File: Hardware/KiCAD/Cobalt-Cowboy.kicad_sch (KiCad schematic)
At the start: 1 part, among them J3 USB_C_Receptacle

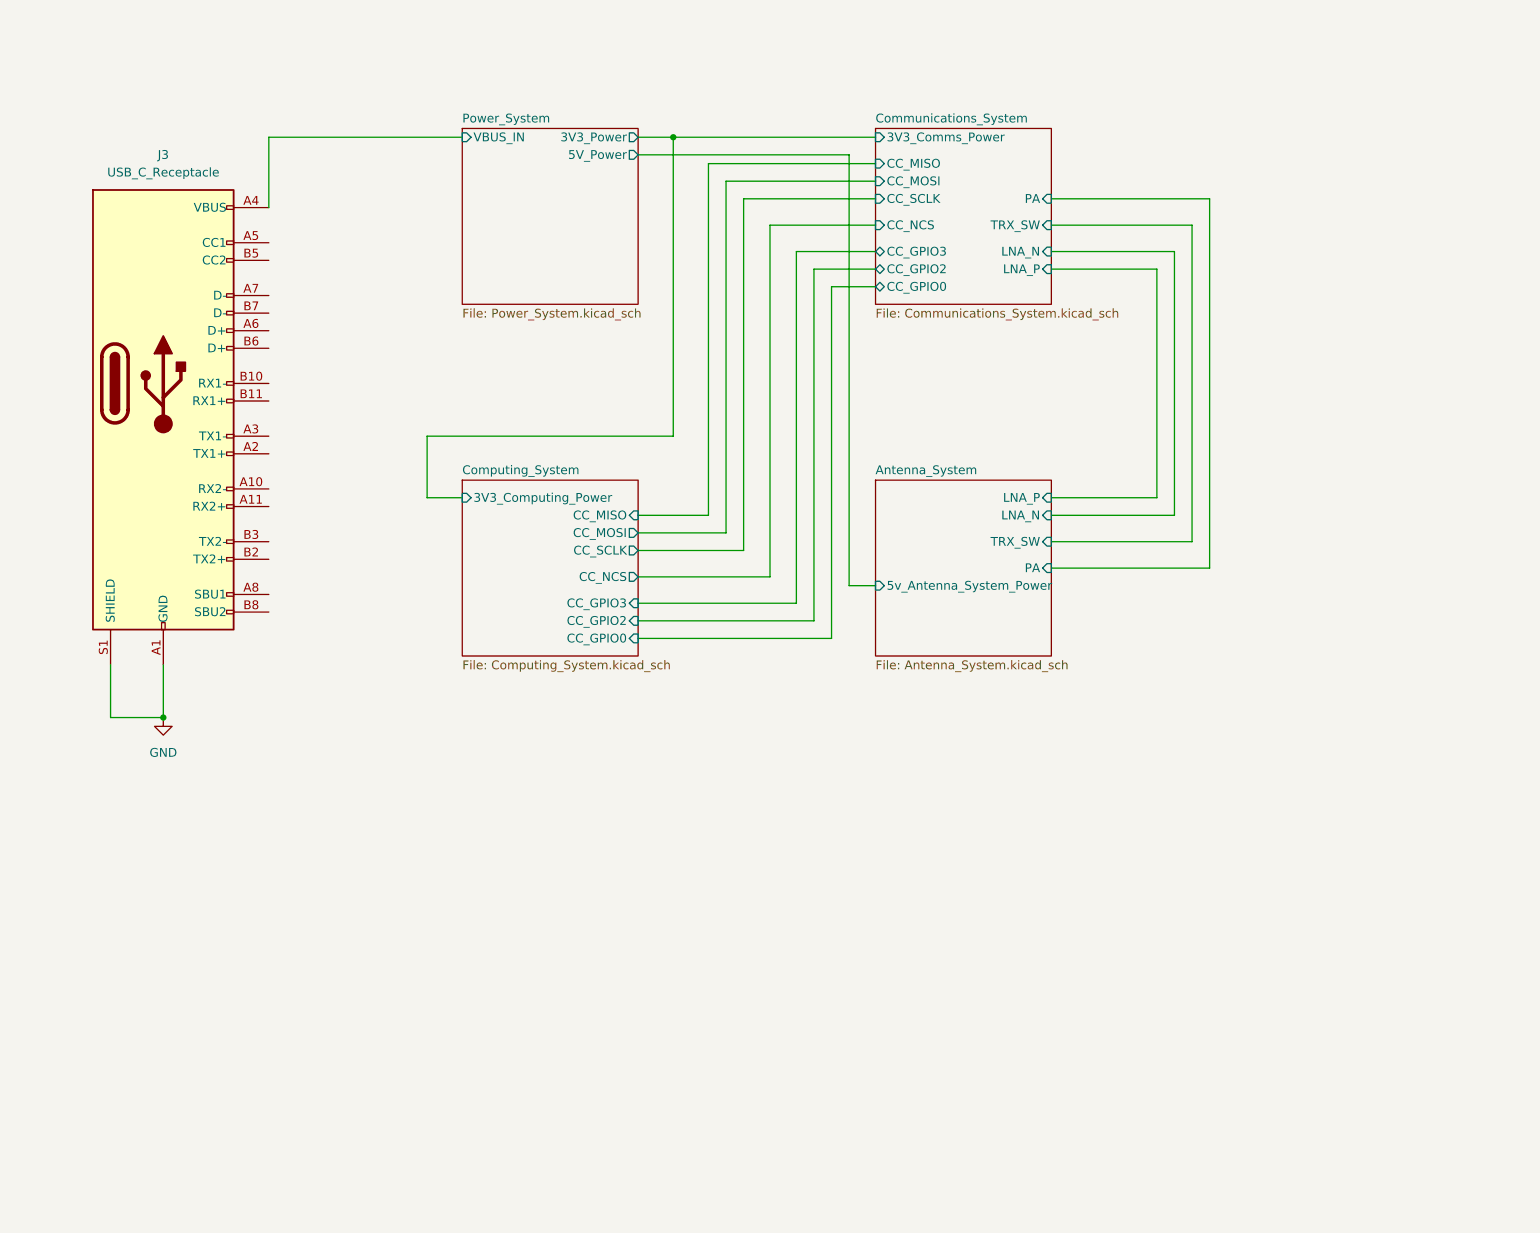
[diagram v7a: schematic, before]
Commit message: feat: subsystem exploration, begin placement, routing #11 #12 #4 many new project symbols
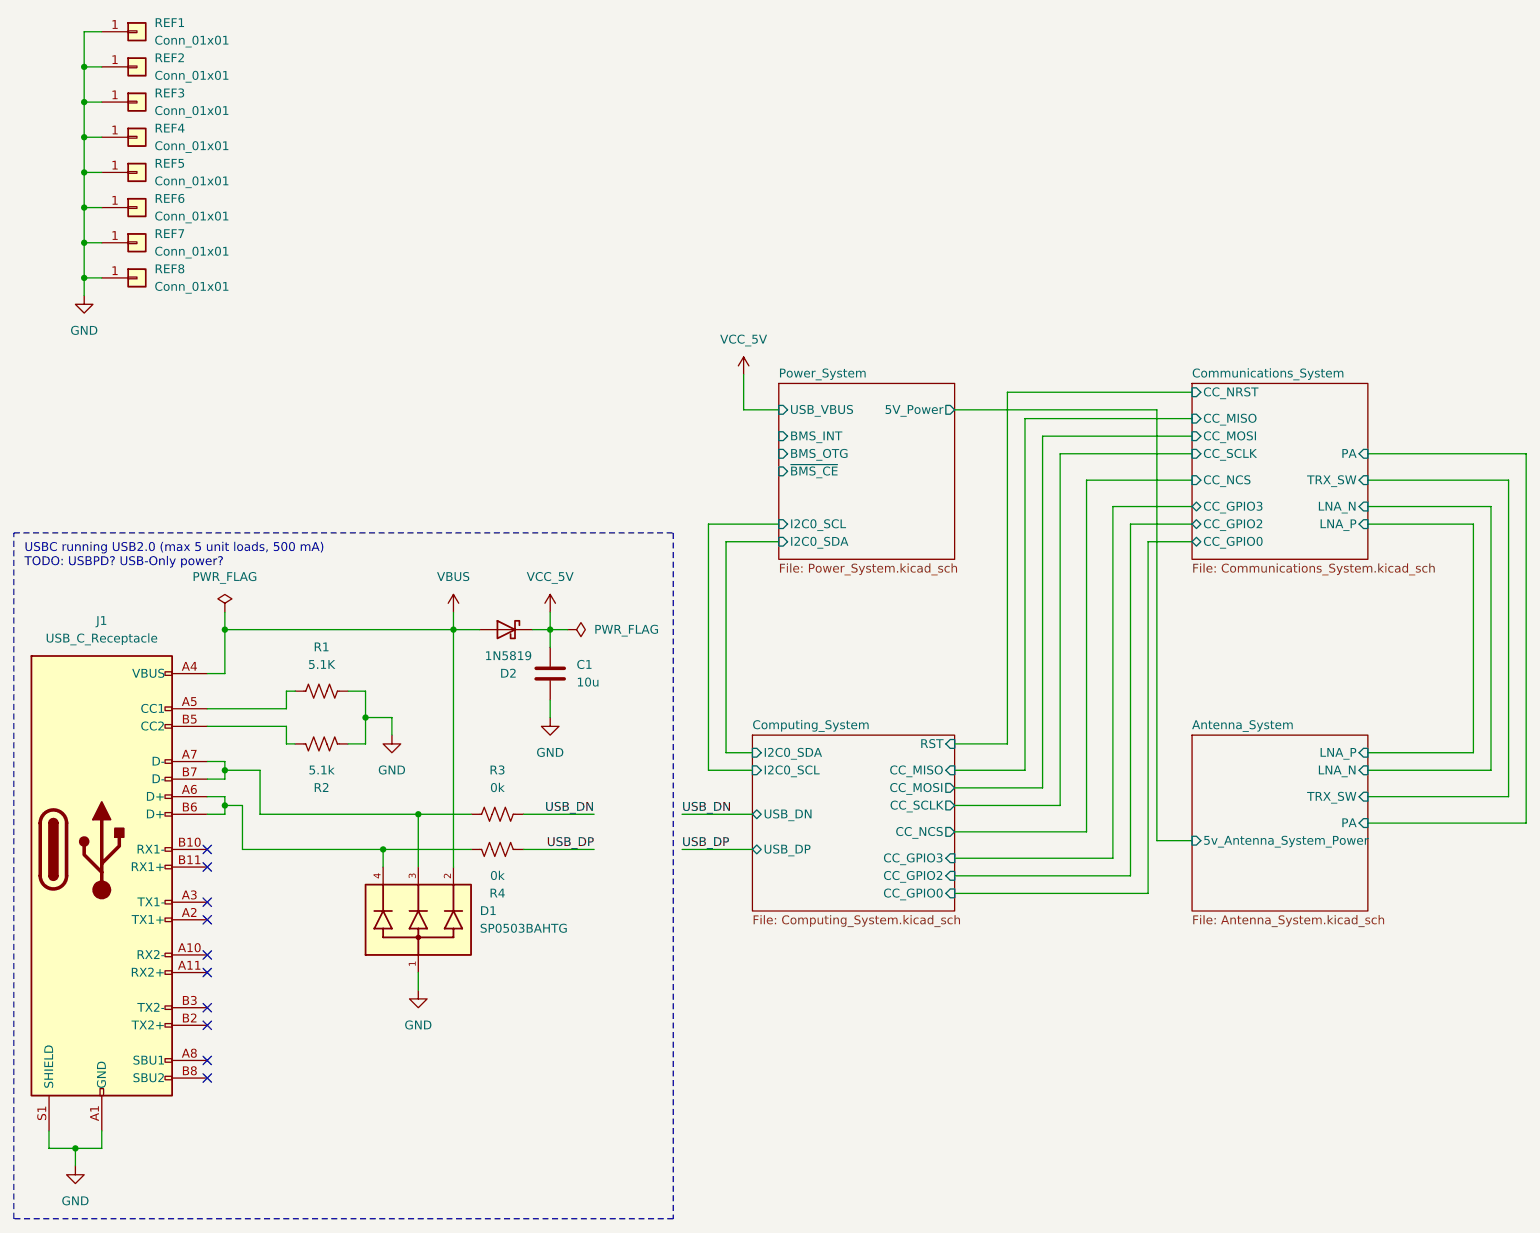
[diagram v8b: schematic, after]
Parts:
- added C1: 10u, Capacitor_SMD:C_0603_1608Metric, symbol Device:C
- added D1: SP0503BAHTG, Cobalt_Cowboy:SOT143, symbol Cobalt-Cowboy:SP0503BAHTG
- added D2: 1N5819, Diode_SMD:D_0603_1608Metric, symbol Diode:1N5819
- added R1: 5.1K, Resistor_SMD:R_0603_1608Metric, symbol Device:R_US
- added R2: 5.1k, Resistor_SMD:R_0603_1608Metric, symbol Device:R_US
- added R3, R4: 0k, Resistor_SMD:R_0603_1608Metric, symbol Device:R_US
- added REF1, REF2, REF3, REF4, REF5, REF6, REF7, REF8: Conn_01x01, MountingHole:MountingHole_2.2mm_M2_Pad_Via, symbol Connector_Generic:Conn_01x01
- J1: renamed from J3; footprint Connector_USB:USB_C_Receptacle_GCT_USB4085 -> Connector_USB:USB_C_Receptacle_GCT_USB4105-xx-A_16P_TopMnt_Horizontal
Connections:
- net GND: now also C1.2, D1.1, R1.1, R2.1, REF1.1 (Pin_1), REF2.1 (Pin_1), REF3.1 (Pin_1), REF4.1 (Pin_1), REF5.1 (Pin_1), REF6.1 (Pin_1), REF7.1 (Pin_1), REF8.1 (Pin_1)
- net at J1.A5 (CC1): now also R1.2
- net at J1.A6 (D+): now also J1.B6 (D+), D1.4, R4.2
- net at J1.A7 (D-): now also J1.B7 (D-), D1.3, R3.1
- net at J1.B5 (CC2): now also R2.2
- net Power_System/VBUS_IN renamed VBUS
- net VBUS: now also D1.2, D2.2 (A)
- new net USB_DN: R3.2
- new net USB_DP: R4.1
- new net VCC_5V: C1.1, D2.1 (K)
- no-connect marks 0 -> 10
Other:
- sheet Communications_System ports: added CC_NRST; removed 3V3_Comms_Power
- sheet Computing_System ports: added I2C0_SCL, I2C0_SDA, RST, USB_DN, USB_DP; removed 3V3_Computing_Power
- sheet Power_System ports: added BMS_INT, BMS_OTG, I2C0_SCL, I2C0_SDA, USB_VBUS, ~{BMS_CE}; removed 3V3_Power, VBUS_IN
- note added: "USBC running USB2.0 (max 5 unit loads, 500 mA) TODO: USBPD? USB-Only power?"
- moved on the sheet: J1
